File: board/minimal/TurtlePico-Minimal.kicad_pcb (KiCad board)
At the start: 2 copper layers, 52.1 x 59.7 mm, 120 parts, among them IC1 DRV8835DSSR, J1 Micro_SD, J10 LED, J11 LED, J12 Debug, J13 9DoF, J14 Temperature, J15 UltraSonic, J16 OLED, J17 5077CR-16SMC2-BK-TR, J3 FR_ESC, J4 FL_ESC, J5 RMotor, J6 LMotor, J7 RR_ESC, J8 RL_ESC, J9 AudioJack3, Q1 PMOS, Q2 PMOS, Q3 PMOS, Q4 PMOS, Q5 2SC4213, Q6 2SC4213, SW1 SW_Bootsel, SW2 SW_RST, SW3 SW_{R}, SW4 SW_{L}, SW5 SW_DIP_x03, U1 W25Q128JVS, U10 PCM5102A, U2 AP63203WU, U3 RP2040, U4 STUSB4500QTR, U5 TLV73318PDBV, U6 PCA9306D, U7 ICM-20948, U8 BME280, U9 INA260, Y1 ABLS-12.000MHZ-B4-T

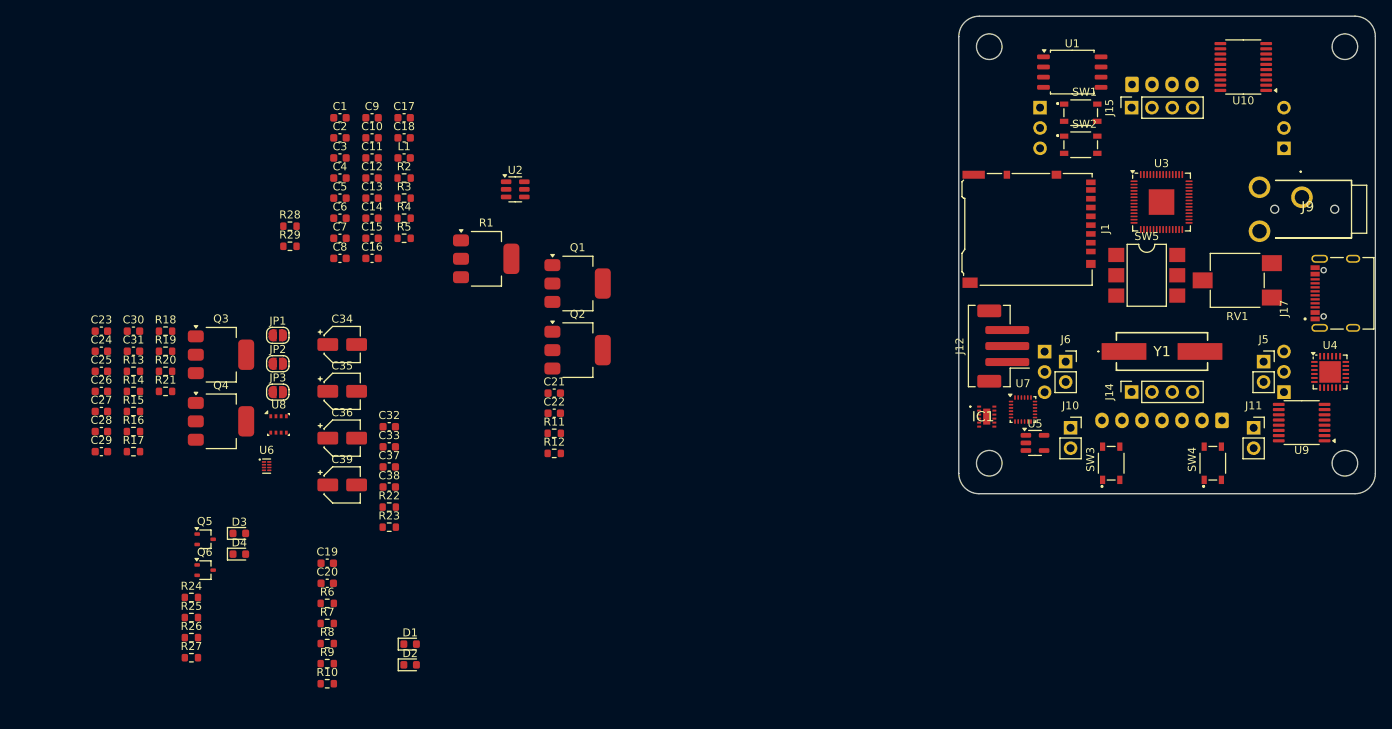
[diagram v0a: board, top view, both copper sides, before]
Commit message: add Weather to Dashboard
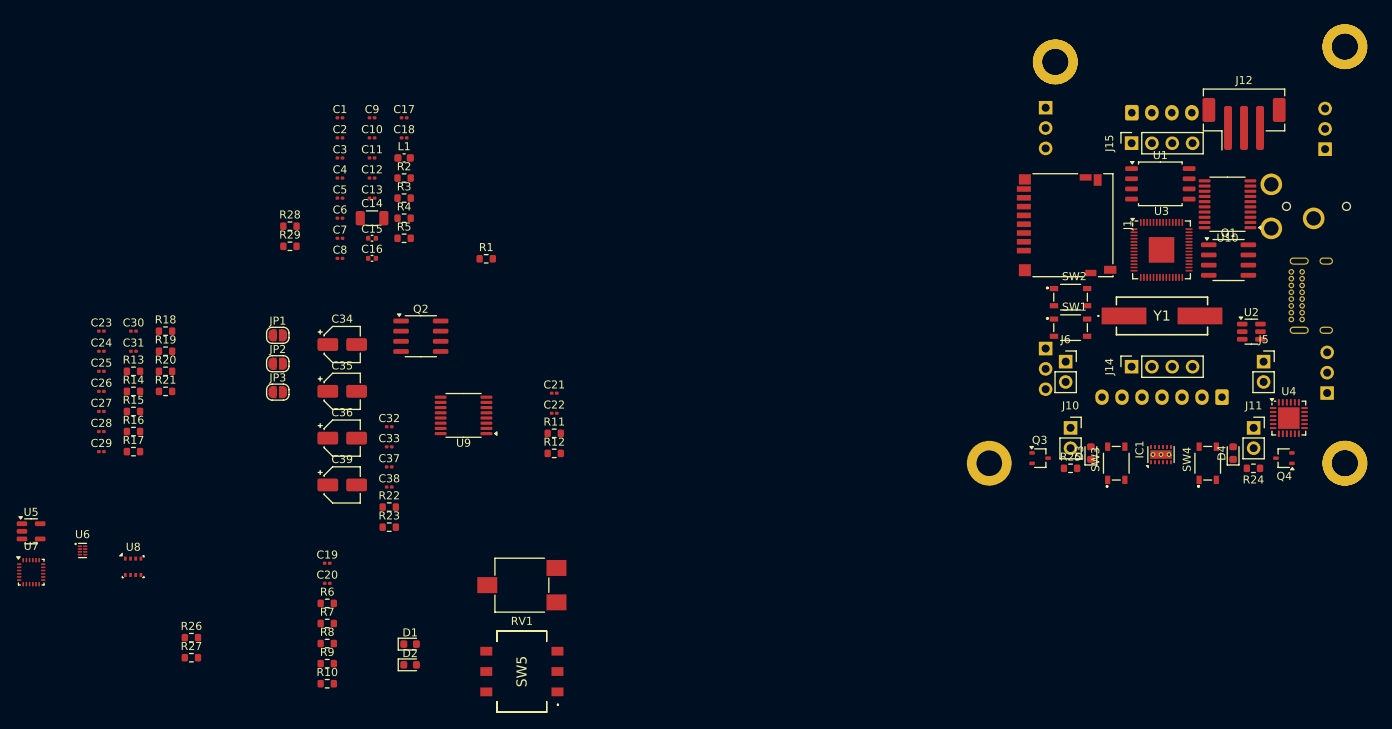
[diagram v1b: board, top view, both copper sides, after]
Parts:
- removed the ? at (212.1, 105.4)
- removed the ? at (212.1, 53.3)
- removed J17: 5077CR-16SMC2-BK-TR, NELTRON_5077CR-16SMC2-BK-TR:NELTRON_5077CR-16SMC2-BK-TR
- removed the Q3 at (116.1, 91.8)
- removed the Q4 at (116.1, 100.2)
- added ?: , , F.Cu at (220.3, 55.2)
- added J2: USB_C_Receptacle_USB2.0_16P, Connector_USB:USB_C_Receptacle_GCT_USB4085, B.Cu at (249.8, 81.5)
- added REF**: MountingHole_3.2mm_M3_DIN965_Pad, MountingHole:MountingHole_3.2mm_M3_DIN965_Pad, F.Cu at (220.3, 55.2)
- added REF**: MountingHole_3.2mm_M3_DIN965_Pad, MountingHole:MountingHole_3.2mm_M3_DIN965_Pad, F.Cu at (256.5, 105.4)
- added REF**: MountingHole_3.2mm_M3_DIN965_Pad, MountingHole:MountingHole_3.2mm_M3_DIN965_Pad, F.Cu at (212.1, 105.4)
- added REF**: MountingHole_3.2mm_M3_DIN965_Pad, MountingHole:MountingHole_3.2mm_M3_DIN965_Pad, F.Cu at (256.5, 53.3)
- C1, C10, C11, C12, C13, C17, C18, C19, C2, C20, C21, C22, C23, C24, C25, C26, C27, C28, C29, C3, C30, C31, C32, C33, C37, C38, C4, C5, C6, C7, C8, C9: footprint Capacitor_SMD:C_0603_1608Metric -> Capacitor_SMD:C_0201_0603Metric
- C14: footprint Capacitor_SMD:C_0603_1608Metric -> Capacitor_SMD:C_1206_3216Metric
- C15, C16: footprint Capacitor_SMD:C_0603_1608Metric -> Capacitor_SMD:C_0402_1005Metric
- IC1: footprint DRV8835:DRV8835DSSR -> Package_SON:WSON-12-1EP_3x2mm_P0.5mm_EP1x2.65_ThermalVias
- J1: footprint Connector_Card:microSD_HC_Hirose_DM3AT-SF-PEJM5 -> Connector_Card:microSD_HC_Hirose_DM3D-SF
- J9: moved to B.Cu
- Q1, Q2: value PMOS -> DMP6050SSD; footprint Package_TO_SOT_SMD:SOT-223 -> Package_SO:SOIC-8_3.9x4.9mm_P1.27mm
- R1: footprint Package_TO_SOT_SMD:SOT-223 -> Resistor_SMD:R_0603_1608Metric
- SW5: footprint Package_DIP:SMDIP-6_W7.62mm -> DS04254203BKSMT:DS04254203BKSMT
- moved Q4 135.6 mm to (248.9, 104.8), turned to 180 degrees
- moved R24 133.7 mm to (245.1, 106.0), turned to 180 degrees
- moved U5 126.0 mm to (92.3, 113.9)
- moved U7 125.6 mm to (92.3, 119.0)
- moved D4 124.9 mm to (242.6, 104.1), turned to 90 degrees
- moved R25 111.5 mm to (222.2, 106.0)
- moved D3 106.9 mm to (224.8, 104.1), turned to 90 degrees
- moved Q3 104.9 mm to (218.4, 104.8)
- moved U9 104.8 mm to (146.4, 99.4)
- moved RV1 97.2 mm to (153.7, 120.7)
- moved U2 93.7 mm to (244.9, 89.0)
- moved SW5 92.5 mm to (153.7, 131.4), turned to 90 degrees
- moved Q1 81.4 mm to (242.0, 80.0)
- moved J12 40.9 mm to (243.9, 63.0), turned to 0 degrees
- moved SW1 26.9 mm to (222.2, 88.5)
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- renumbered Q5 to Q3, Q6 to Q4
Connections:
- Q1 pad 1: +3.3V -> Net-(Q1A-S1)
- Q1 pad 3: Net-(Q1-S) -> Net-(Q1A-S1)
- Q1 pad 4: (no net) -> Net-(J3-Pin_2)
- Q2 pad 1: Net-(J3-Pin_2) -> Net-(Q2A-S1)
- Q2 pad 2: Net-(J3-Pin_2) -> PW_EN
- Q2 pad 3: Net-(Q1-S) -> Net-(Q2A-S1)
- Q2 pad 4: (no net) -> PW_EN
- R11 pad 2: Net-(Q1-S) -> Net-(Q1A-S1)
- R20 pad 1: Net-(Q3-S) -> Net-(Q2A-S1)
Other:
- board outline removed
